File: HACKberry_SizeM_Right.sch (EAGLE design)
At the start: 14 parts, among them IC1 OKI-78SR-5_1.5-W36H-C

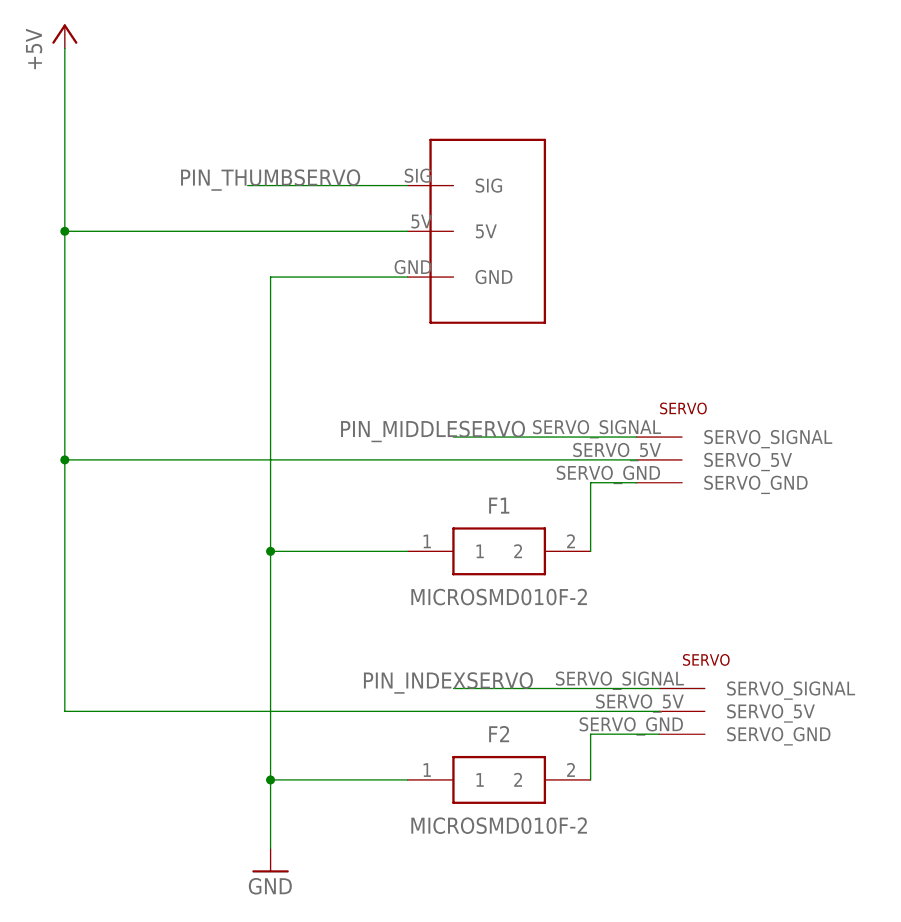
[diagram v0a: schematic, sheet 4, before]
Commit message: ポリスイッチを取り除き, サーボの電源ラインにパスコンを追加した.
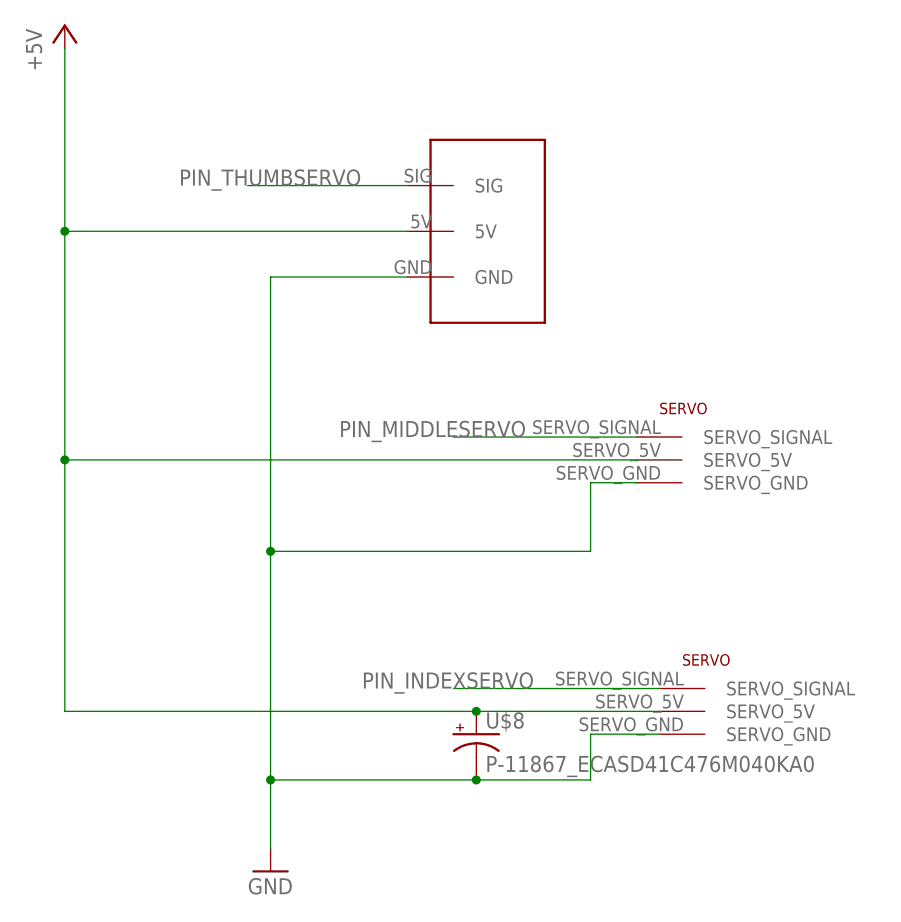
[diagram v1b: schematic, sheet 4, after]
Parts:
- removed F1, F2: MICROSMD010F-2, HbHandBoard_SizeM:MICROSMD010F-2
- added U$8: P-11867_ECASD41C476M040KA0, Akizuki:P-11867_ECASD41C476M040KA0
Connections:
- removed net N$2: F1.2, MIDDLEPIN.SERVO_GND
- removed net N$3: F2.2, INDEXPIN.SERVO_GND
- net +5V: now also U$8.+
- net GND: now also INDEXPIN.SERVO_GND, MIDDLEPIN.SERVO_GND, U$8.-; no longer F1.1, F2.1
